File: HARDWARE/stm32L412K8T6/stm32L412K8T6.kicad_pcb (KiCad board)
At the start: 2 copper layers, 53.9 x 70.5 mm, 27 parts, among them J1 Conn_01x02, J2 Conn_01x03_Male, J4 Conn_01x03_Male, J5 Conn_01x03_Male, J6 Conn_01x03_Male, U1 STM32L011K3Tx, U2 AMS1117-3.3, Y1 Crystal

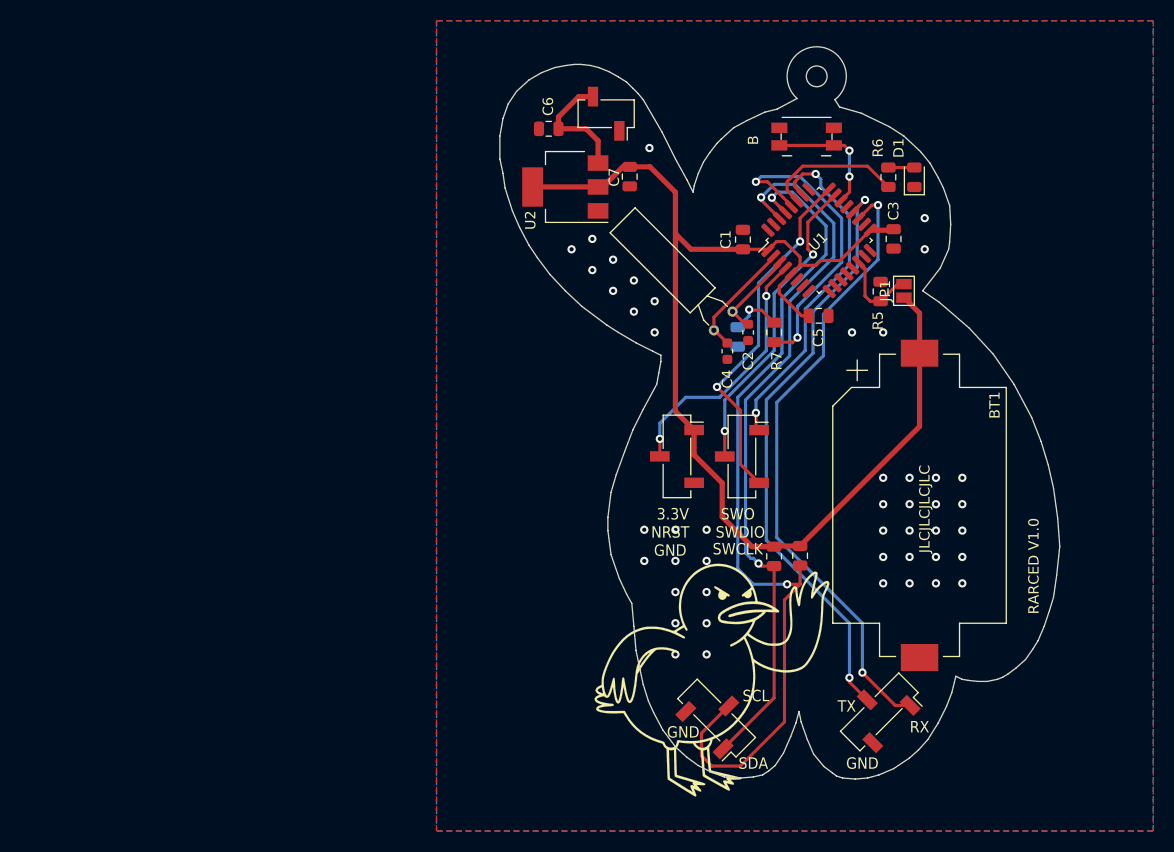
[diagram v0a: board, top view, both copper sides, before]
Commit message: fail in processing gerber, create a new board
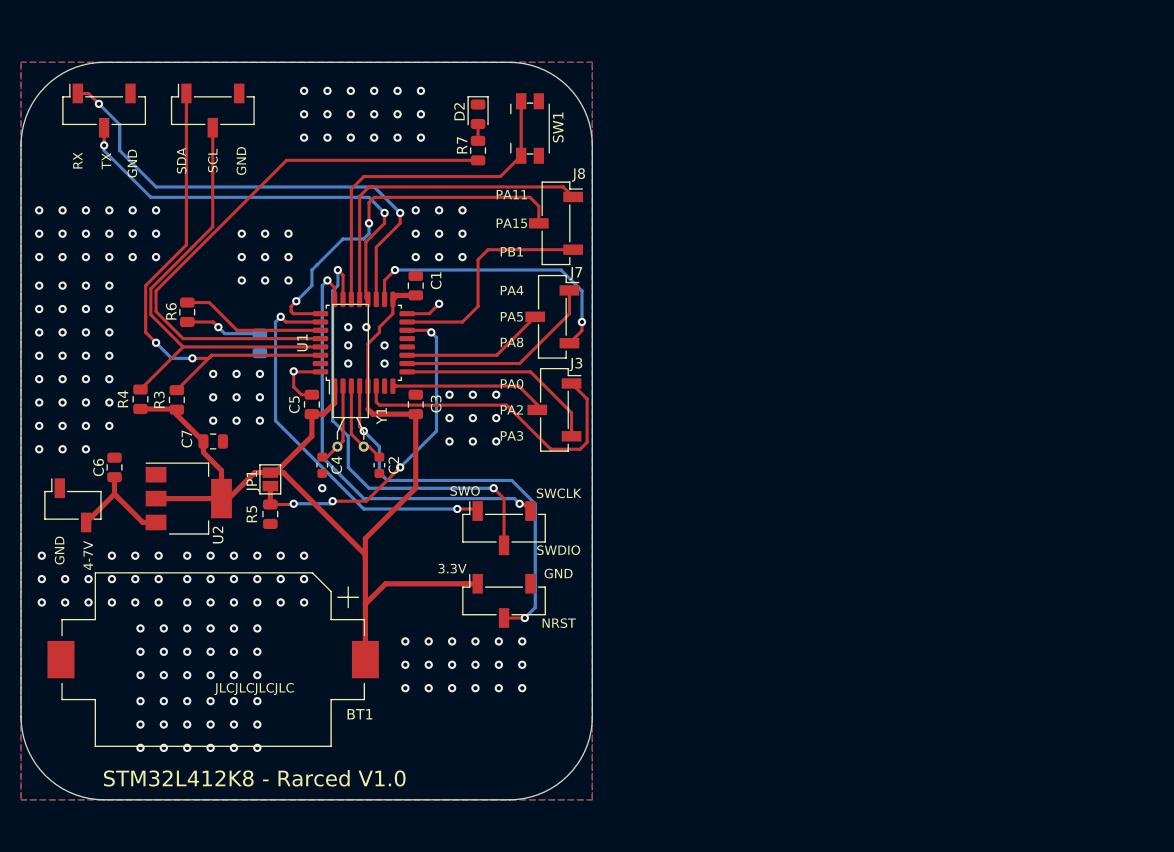
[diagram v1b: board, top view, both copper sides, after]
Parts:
- removed B: SW_Push, Button_Switch_SMD:Panasonic_EVQPUJ_EVQPUA
- removed the G*** at (182.2, 115.8)
- added J3: Conn_01x03_Male, Connector_PinSocket_2.54mm:PinSocket_1x03_P2.54mm_Vertical_SMD_Pin1Right, F.Cu at (167.3, 90.5)
- added J7: Conn_01x03_Male, Connector_PinSocket_2.54mm:PinSocket_1x03_P2.54mm_Vertical_SMD_Pin1Right, F.Cu at (167.2, 81.5)
- added J8: Conn_01x03_Male, Connector_PinSocket_2.54mm:PinSocket_1x03_P2.54mm_Vertical_SMD_Pin1Right, F.Cu at (167.5, 72.5)
- added SW1: SW_Push, Button_Switch_SMD:Panasonic_EVQPUJ_EVQPUA, F.Cu at (165.0, 63.4)
- D1: moved to B.Cu
- D2: moved to F.Cu
- moved J2 94.4 mm to (124.0, 61.6), turned to 90 degrees
- moved J5 76.0 mm to (134.5, 61.6), turned to 90 degrees
- moved BT1 69.6 mm to (134.5, 114.5), turned to 180 degrees
- moved R6 68.7 mm to (132.0, 81.1), turned to 270 degrees
- moved R4 65.3 mm to (127.5, 89.4), turned to 90 degrees
- moved D1 65.0 mm to (139.0, 84.1)
- moved J1 63.7 mm to (121.0, 99.7), turned to 90 degrees
- moved JP1 63.6 mm to (140.0, 97.2), turned to 270 degrees
- moved R5 62.5 mm to (140.0, 100.5), turned to 270 degrees
- moved R3 59.4 mm to (131.0, 89.5), turned to 90 degrees
- moved C6 53.0 mm to (125.0, 96.0), turned to 90 degrees
- moved C5 49.5 mm to (144.0, 89.9), turned to 90 degrees
- moved C3 48.7 mm to (154.0, 89.9), turned to 90 degrees
- moved C7 47.5 mm to (134.5, 93.5), turned to 0 degrees
- moved U2 47.1 mm to (132.2, 99.0), turned to 0 degrees
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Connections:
- U1 pad 10: (no net) -> PA4
- U1 pad 11: (no net) -> PA5
- U1 pad 15: (no net) -> PB1
- U1 pad 18: (no net) -> PA8
- U1 pad 21: (no net) -> PA11
- U1 pad 25: (no net) -> PA15
- U1 pad 6: (no net) -> PA0
- U1 pad 8: (no net) -> PA2
- U1 pad 9: (no net) -> PA3
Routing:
- net SCL: track 84.5 -> 43.9 mm, vias 2 -> 0
- net PA15: track 0.00 -> 36.2 mm, vias 0 -> 2
- net PA11: track 0.00 -> 31.2 mm
- net PA0: track 0.00 -> 30.3 mm
- net PA8: track 0.00 -> 27.6 mm, vias 0 -> 2
- net LED_GREEN: track 30.3 -> 55.1 mm, vias 2 -> 0
- net BOOT0: track 8.92 -> 32.8 mm, vias 0 -> 4
- net SDA: track 70.0 -> 47.4 mm
- net PB1: track 0.00 -> 21.5 mm
- net BUTTON: track 12.1 -> 33.6 mm, vias 2 -> 0
- net PA4: track 0.00 -> 19.9 mm
- net PA3: track 0.00 -> 19.7 mm
- net TX: track 57.8 -> 40.9 mm
- net PA2: track 0.00 -> 15.2 mm
- net RX: track 60.8 -> 46.5 mm
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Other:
- board size 53.9 x 70.5 mm -> 55 x 71 mm
- board text added: "4-7V"
- board text added: "B"
- board text added: "PA0"
- board text added: "PA11"
- board text added: "PA15"
- board text added: "PA2"
- board text added: "PA3"
- board text added: "PA4"
- board text added: "PA5"
- board text added: "PA8"
- board text added: "PB1"
- board text added: "STM32L412K8 - Rarced V1.0"
- board text removed: "RARCED V1.0"
